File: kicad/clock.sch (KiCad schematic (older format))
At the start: 17 parts, among them P1 CONN_01X03, SW1 SWITCH_MIN, SW2 SWITCH_HR, U1 74LS90, U10 74LS247, U11 74LS73, U2 74LS90, U3 MAX6817, U4 74LS90, U5 74LS247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

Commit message: Add bypass caps and route VCC
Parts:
- added C1, C2: 22μF, Capacitors_SMD:C_0805_HandSoldering, symbol C
- renumbered C1 to C3, U8 to U7, U7 to U8
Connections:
- net GND: now also C1.2, C2.2
- net VCC: now also C1.1, C2.1
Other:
- note added: "C2012X6S0J226M085AC"
- moved on the sheet: C3, D1, P1, R1, SW1, SW2, U1, U2, U3

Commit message: Complete layout, pass DRC, create gerbers
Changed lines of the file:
@@
 Sheet 1 2
 Title "Clock"
-Date "2016-07-17"
-Rev "A"
+Date "2017-03-19"
+Rev "0.1"
 Comp "Scalez Inc."
 Comment1 ""
@@
 Connection ~ 16150 7500
 Wire Wire Line
-	16050 7500 16150 7500
-Wire Wire Line
-	16150 7500 16450 7500
+	16050 7500 16450 7500
 Wire Wire Line
 	16200 7300 17050 7300
@@
 	16100 8300 16100 6950
 Wire Wire Line
-	16050 7800 16200 7800
-Wire Wire Line
-	16200 7800 16450 7800
+	16050 7800 16450 7800
 Wire Wire Line
 	16450 7700 16050 7700
@@
 	16800 6850 16850 6850
 Wire Wire Line
-	16800 6600 16800 6650
-Wire Wire Line
-	16800 6650 16800 6850
+	16800 6600 16800 6850
 Wire Wire Line
 	16850 6650 16800 6650
@@
 	16850 6050 16650 6050
 Wire Wire Line
-	13450 7000 13450 7050
-Wire Wire Line
-	13450 7050 13450 7250
+	13450 7000 13450 7250
 Wire Wire Line
 	13500 7050 13450 7050
@@
 	11250 7700 11300 7700
 Wire Wire Line
-	11250 7450 11250 7500
-Wire Wire Line
-	11250 7500 11250 7700
+	11250 7450 11250 7700
 Wire Wire Line
 	11300 7500 11250 7500
 Wire Bus Line
-	11000 7000 11000 7100
-Wire Bus Line
-	11000 7100 11000 7200
-Wire Bus Line
-	11000 7200 11000 7300
-Wire Bus Line
-	11000 7300 11000 7600
-Wire Bus Line
-	11000 7600 11000 7700
-Wire Bus Line
-	11000 7700 11000 7800
-Wire Bus Line
-	11000 7800 11000 7900
+	11000 7000 11000 7900
 Wire Wire Line
 	11300 7000 11100 7000
@@
 	3150 7350 3100 7350
 Wire Wire Line
-	3100 7350 3100 7450
-Wire Wire Line
-	3100 7450 3100 7600
-Wire Wire Line
-	3100 7600 3100 7700
-Wire Wire Line
-	3100 7700 3100 7750
+	3100 7350 3100 7750
 Wire Wire Line
 	3100 7450 3150 7450
@@
 	11150 8350 11300 8350
 Wire Wire Line
-	9050 7950 9050 8050
-Wire Wire Line
-	9050 8050 9050 8200
-Wire Wire Line
-	9050 8200 9050 8300
-Wire Wire Line
-	9050 8300 9050 8350
+	9050 7950 9050 8350
 Connection ~ 9050 8050
 Connection ~ 9050 8200
@@
 	6400 7200 6400 7600
 Wire Wire Line
-	6250 7600 6400 7600
-Wire Wire Line
-	6400 7600 6700 7600
+	6250 7600 6700 7600
 Wire Wire Line
 	4750 7300 4750 7500
@@
 	4750 7500 4800 7500
 Wire Wire Line
-	4750 7900 4750 8000
-Wire Wire Line
-	4750 8000 4750 8050
+	4750 7900 4750 8050
 Wire Wire Line
 	3150 7200 3100 7200
@@
 	9050 7600 9050 7800
 Wire Wire Line
-	10550 7700 10600 7700
-Wire Wire Line
-	10600 7700 10900 7700
+	10550 7700 10900 7700
 Wire Wire Line
 	11300 8100 11250 8100
@@
 	11250 8100 11250 7900
 Wire Wire Line
-	12750 8000 12800 8000
-Wire Wire Line
-	12800 8000 13150 8000
-Wire Wire Line
-	10550 8000 10900 8000
-Wire Wire Line
-	10900 8000 11300 8000
+	12750 8000 13150 8000
+Wire Wire Line
+	10550 8000 11300 8000
 Connection ~ 6400 7600
 Wire Wire Line
 	4600 7400 4800 7400
 Wire Wire Line
-	2750 7100 3000 7100
-Wire Wire Line
-	3000 7100 3150 7100
+	2750 7100 3150 7100
 Wire Wire Line
 	10550 7900 10900 7900
@@
 	11200 7850 12850 7850
 Wire Wire Line
-	12750 8100 12850 8100
-Wire Wire Line
-	12850 8100 13150 8100
+	12750 8100 13150 8100
 Wire Wire Line
 	11150 8350 11150 7800
@@
 	12900 7800 12900 8200
 Wire Wire Line
-	11250 8500 11250 8600
-Wire Wire Line
-	11250 8600 11250 8650
+	11250 8500 11250 8650
 Connection ~ 12900 8200
 Wire Bus Line
-	13250 6550 13250 6650
-Wire Bus Line
-	13250 6650 13250 6750
-Wire Bus Line
-	13250 6750 13250 7900
-Wire Bus Line
-	13250 7900 13250 8000
-Wire Bus Line
-	13250 8000 13250 8100
-Wire Wire Line
-	14600 7500 14600 7600
-Wire Wire Line
-	14600 7600 14600 7700
-Wire Wire Line
-	14350 7500 14600 7500
-Wire Wire Line
-	14600 7500 14650 7500
+	13250 6550 13250 8100
+Wire Wire Line
+	14600 7500 14600 7700
+Wire Wire Line
+	14350 7500 14650 7500
 Wire Wire Line
 	14600 7600 14650 7600
@@
 	14500 8100 14650 8100
 Wire Wire Line
-	14500 7750 14500 7800
-Wire Wire Line
-	14500 7800 14500 8100
-Wire Wire Line
-	14500 8100 14500 8200
+	14500 7750 14500 8200
 Wire Wire Line
 	14500 7800 14650 7800
@@
 Connection ~ 14500 8100
 Wire Wire Line
-	16050 7600 16150 7600
-Wire Wire Line
-	16150 7600 16450 7600
+	16050 7600 16450 7600
 Wire Wire Line
 	14550 8000 14650 8000
@@
 Connection ~ 16150 7600
 Wire Bus Line
-	16550 6150 16550 6250
+	16550 6150 16550 6500
 Wire Bus Line
-	16550 6250 16550 6350
-Wire Bus Line
-	16550 6350 16550 6450
-Wire Bus Line
-	16550 6450 16550 6500
-Wire Bus Line
-	16550 6450 16550 7400
-Wire Bus Line
-	16550 7400 16550 7500
-Wire Bus Line
-	16550 7500 16550 7600
-Wire Bus Line
-	16550 7600 16550 7700
+	16550 6450 16550 7700
 Wire Wire Line
 	16150 7100 17050 7100
@@
 	19650 7100 19700 7100
 Wire Wire Line
-	19650 7100 19650 7500
-Wire Wire Line
-	19650 7500 19650 7900
-Wire Wire Line
-	19650 7900 19650 8000
-Wire Wire Line
-	19650 8000 19650 8400
-Wire Wire Line
-	19650 8400 19650 8800
+	19650 7100 19650 8800
 Wire Wire Line
 	19650 7500 19700 7500
@@
 	11300 6900 11100 6900
 Wire Wire Line
-	18250 7200 18300 7200
-Wire Wire Line
-	18300 7200 18400 7200
+	18250 7200 18400 7200
 Connection ~ 18300 7200
 Connection ~ 19650 7900
@@
 	18300 8600 18300 7200
 Wire Wire Line
-	18350 7400 18350 8200
-Wire Wire Line
-	18350 8200 18350 8650
-Wire Wire Line
-	18250 8200 18350 8200
-Wire Wire Line
-	18350 8200 19700 8200
+	18350 7400 18350 8650
+Wire Wire Line
+	18250 8200 19700 8200
 Connection ~ 18350 8200
 Wire Wire Line
@@
 	13300 8200 13250 8200
 Wire Wire Line
-	13250 8200 13250 8400
-Wire Wire Line
-	13250 8400 13250 8800
+	13250 8200 13250 8800
 Wire Wire Line
 	13250 8400 13300 8400
@@
 	7300 7950 7350 7950
 Wire Wire Line
-	6400 7800 6400 8200
-Wire Wire Line
-	6400 8200 6400 8300
+	6400 7800 6400 8300
 Wire Wire Line
 	8650 7700 9100 7700
@@
 	8850 8350 8850 8300
 Wire Wire Line
-	8850 7900 8850 7950
-Wire Wire Line
-	8850 7950 8850 8000
+	8850 7900 8850 8000
 Wire Wire Line
 	8650 7950 8850 7950
@@
 $EndComp
 Wire Wire Line
-	3000 7050 3000 7100
-Wire Wire Line
-	3000 7100 3000 8200
+	3000 7050 3000 8200
 Wire Wire Line
 	3000 6650 3000 6600
@@
 Connection ~ 6400 8200
 Wire Wire Line
-	12750 8200 12900 8200
-Wire Wire Line
-	12900 8200 13150 8200
+	12750 8200 13150 8200
 Text Label 6450 8100 0    60   ~ 0
 mto2
@@
 $EndComp
 Wire Wire Line
-	1900 6850 1900 6800
-Wire Wire Line
-	1900 6800 1800 6800
-Wire Wire Line
-	1800 6800 1700 6800
+	1900 6800 1900 6850
+Wire Wire Line
+	1700 6800 1900 6800
 Wire Wire Line
 	1700 6800 1700 6850
@@
 	1700 7150 1700 7200
 Wire Wire Line
-	1700 7200 1800 7200
-Wire Wire Line
-	1800 7200 1900 7200
+	1700 7200 1900 7200
 Wire Wire Line
 	1900 7200 1900 7150

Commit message: Add notes to schematic and update pcbnew view
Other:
- note added: "Seconds"
- moved on the sheet: C1, C2, C3, D1, P1, R1, SW1, SW2, U1, U10, U11A, U11B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

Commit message: Add BoM, update component info, use 150Ohm current limiting resistors, update layout respectively
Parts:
- C1, C2: Distrib Link (none) -> http://www.digikey.com/product-detail/en/tdk-corporation/C2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; Distrib PN (none) -> 445-14469-1-ND; MFG Name (none) -> TDK; MFG Part Num (none) -> C2012X6S0J226M085AC; Others (none) -> http://www.digikey.com/products/en/capacitors/ceramic-capac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; Tolerance (none) -> 20%
- C3: Distrib Link (none) -> http://www.digikey.com/product-detail/en/tdk-corporation/C2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; Distrib PN (none) -> 445-8883-1-ND; MFG Name (none) -> TDK; MFG Part Num (none) -> C2012X7T2E104K125AE; Others (none) -> http://www.digikey.com/products/en/capacitors/ceramic-capac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; Tolerance (none) -> 10%
- D1: Distrib Link (none) -> http://www.digikey.com/product-detail/en/lite-on-inc/LTST-C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; Distrib PN (none) -> 160-1427-1-ND; MFG Name (none) -> Lite-On; MFG Part Num (none) -> LTST-C171KRKT; Others (none) -> http://www.digikey.com/products/en/optoelectronics/led-indi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; Tolerance (none) -> -
- P1: Distrib Link (none) -> http://www.digikey.com/product-detail/en/molex-llc/07055300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; Distrib PN (none) -> WM4901-ND; MFG Name (none) -> Molex; MFG Part Num (none) -> 0705530002; Others (none) -> -; Tolerance (none) -> -
- R1: value 220Ω -> 150Ω; Distrib Link (none) -> http://www.digikey.com/product-detail/en/stackpole-electron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; Distrib PN (none) -> RMCF0805JT150RCT-ND; MFG Name (none) -> Stackpole Electronics; MFG Part Num (none) -> RMCF0805JT150R; Others (none) -> http://www.digikey.com/products/en/resistors/chip-resistor-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; Tolerance (none) -> 5%
- SW1, SW2: Distrib Link (none) -> http://www.digikey.com/product-detail/en/nkk-switches/AB15A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; Distrib PN (none) -> 360-2706-ND; MFG Name (none) -> NKK Switches; MFG Part Num (none) -> AB15AP-FA; Others (none) -> -; Tolerance (none) -> -
- U1, U2, U4, U6: Distrib Link (none) -> http://www.digikey.com/product-detail/en/texas-instruments/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; Distrib PN (none) -> 296-3746-5-ND; MFG Name (none) -> Texas Instruments; MFG Part Num (none) -> SN74LS90D; Others (none) -> http://www.digikey.com/products/en?keywords=74ls90&stock=1; Tolerance (none) -> -
- U10, U5, U8: Distrib Link (none) -> http://www.digikey.com/product-detail/en/texas-instruments/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; Distrib PN (none) -> 296-38241-1-ND; MFG Name (none) -> Texas Instruments; MFG Part Num (none) -> SN74LS247DR; Others (none) -> http://www.digikey.com/products/en?keywords=74ls247&stock=1; Tolerance (none) -> -
- U11: Distrib Link (none) -> http://www.digikey.com/product-detail/en/texas-instruments/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; Distrib PN (none) -> 296-3742-1-ND; MFG Name (none) -> Texas Instruments; MFG Part Num (none) -> SN74LS73ADR; Others (none) -> http://www.digikey.com/products/en?keywords=74LS73&stock=1; Tolerance (none) -> -
- U3: Distrib Link (none) -> http://www.digikey.com/product-detail/en/maxim-integrated/M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; Distrib PN (none) -> MAX6817EUT+TCT-ND; MFG Name (none) -> Maxim; MFG Part Num (none) -> MAX6817EUT+T; Others (none) -> http://www.digikey.com/products/en?keywords=MAX6817&stock=1; Tolerance (none) -> -
- U7: Distrib Link (none) -> http://www.digikey.com/product-detail/en/texas-instruments/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; Distrib PN (none) -> 296-14873-1-ND; MFG Name (none) -> Texas Instruments; MFG Part Num (none) -> SN74LS00DR; Others (none) -> http://www.digikey.com/products/en?keywords=74ls00&stock=1; Tolerance (none) -> -
- U9: Distrib Link (none) -> http://www.digikey.com/product-detail/en/texas-instruments/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; Distrib PN (none) -> 296-44704-1-ND; MFG Name (none) -> Texas Instruments; MFG Part Num (none) -> SN74LS163ADR; Others (none) -> http://www.digikey.com/products/en?keywords=74ls163&stock=1; Tolerance (none) -> -
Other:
- note removed: "C2012X6S0J226M085AC"

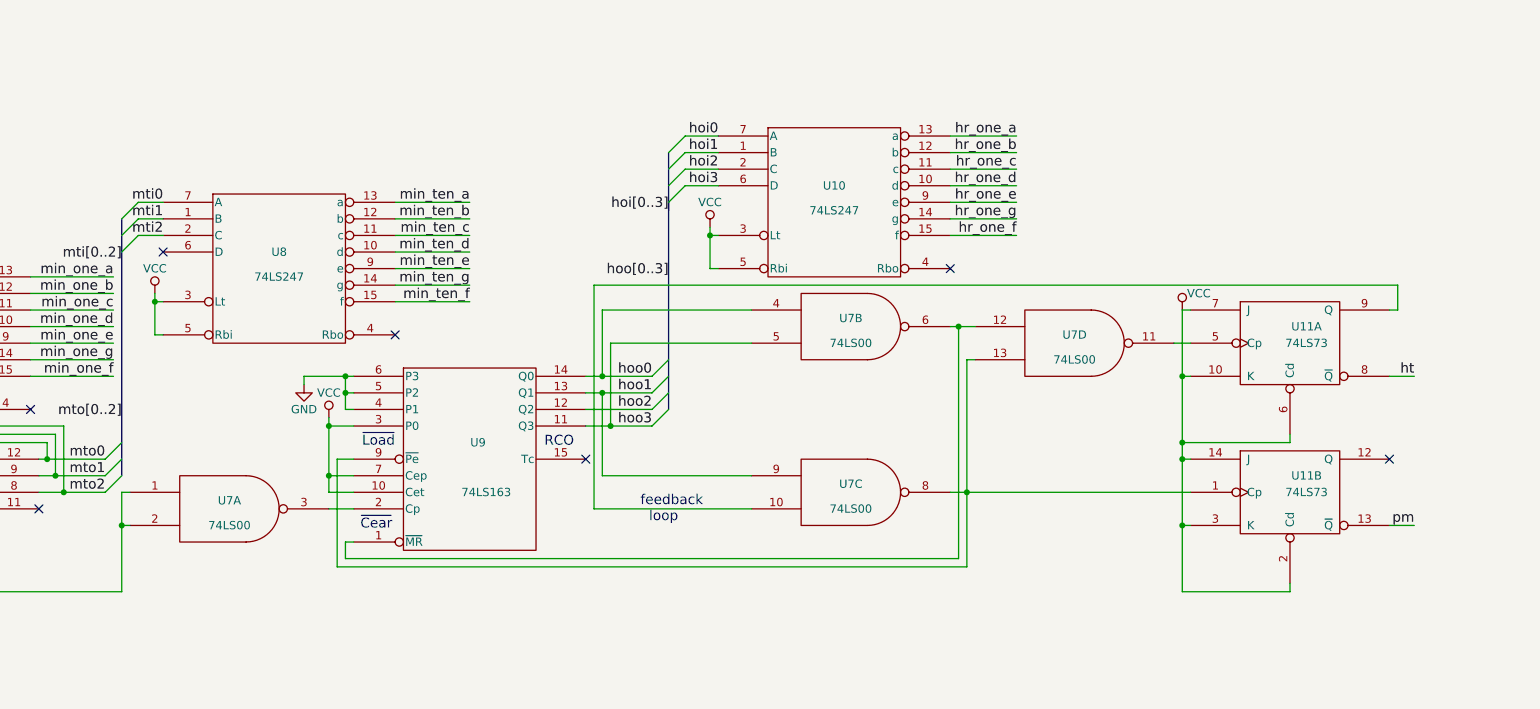
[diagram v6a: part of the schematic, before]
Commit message: Brint input D of U8 to GND
Was floating
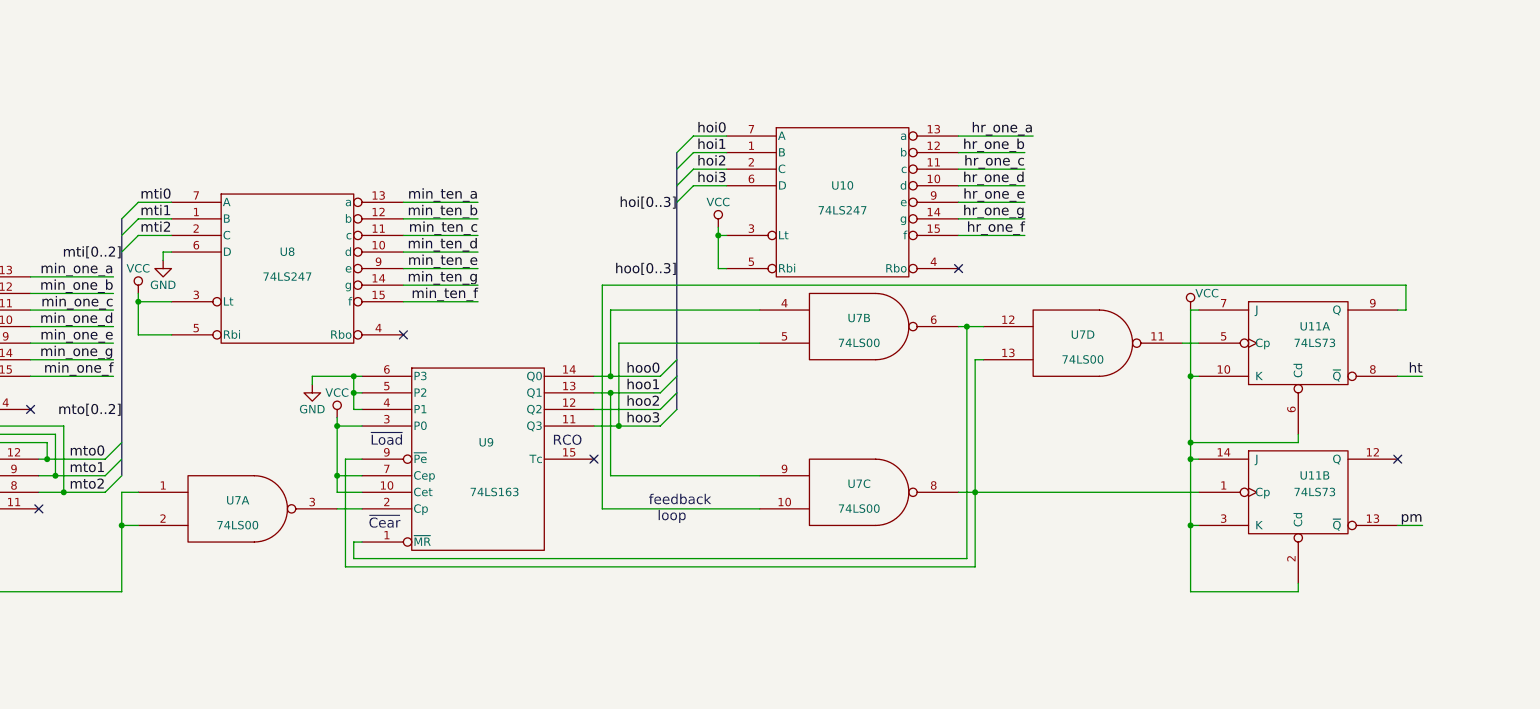
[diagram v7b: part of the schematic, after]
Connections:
- net GND: now also U8.6 (D)
- no-connect marks 10 -> 9
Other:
- moved on the sheet: U10, U11A, U11B, U7A, U7B, U7C, U7D, U8, U9

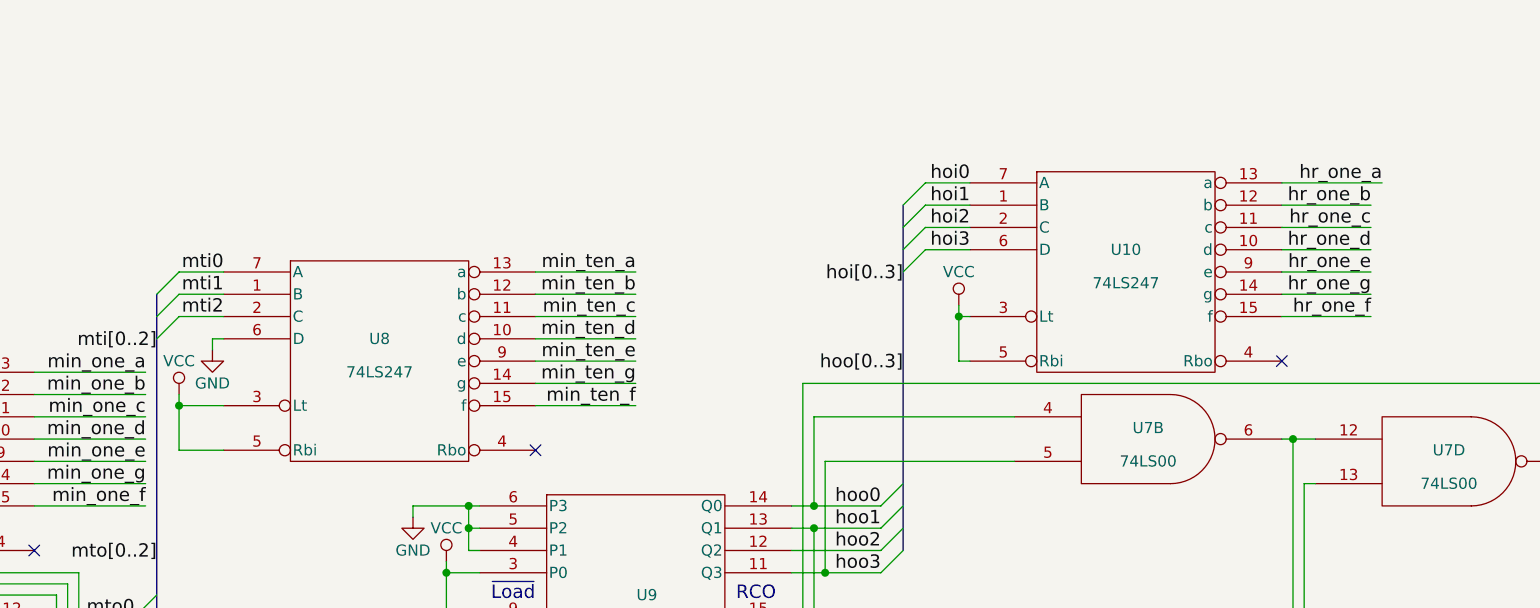
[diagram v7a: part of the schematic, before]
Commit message: Swap pin 1 and 3 of the SPDT push button footprint and update layout accordingly
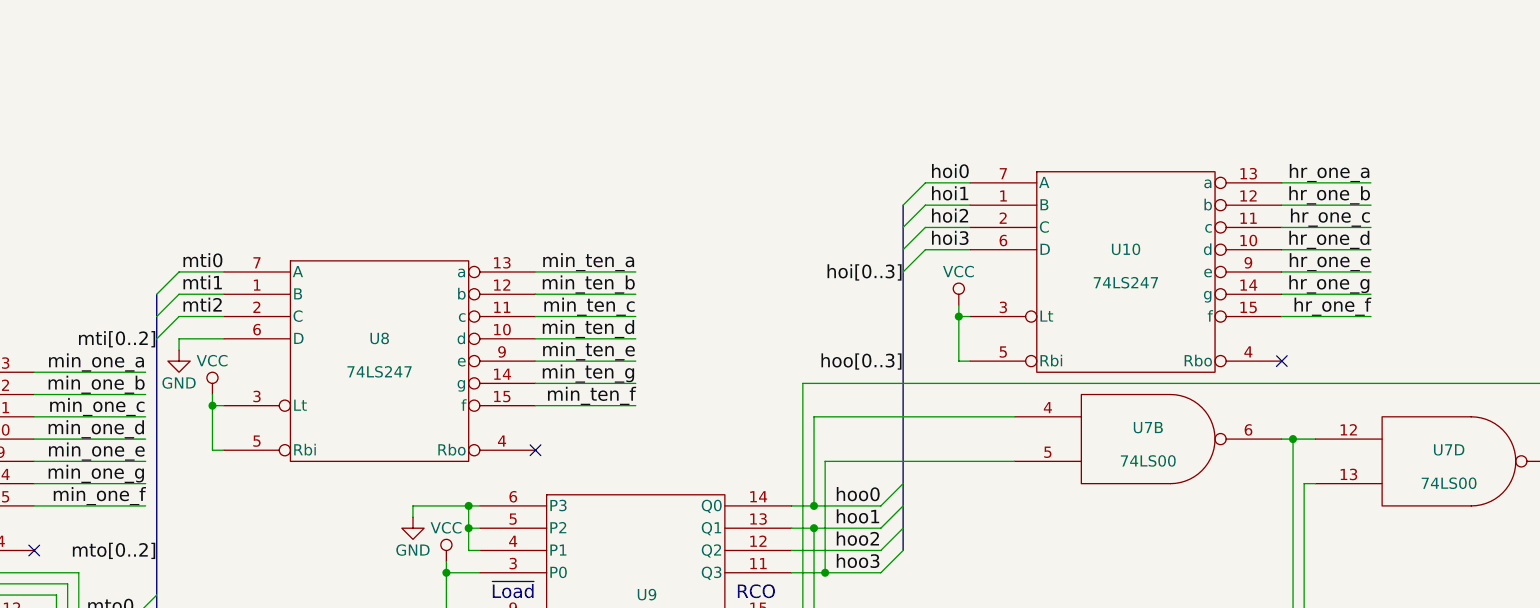
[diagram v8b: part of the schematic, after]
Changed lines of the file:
@@
 Text Label 15500 6950 2    60   ~ 0
 min_ten_g
-Text Label 18850 6050 2    60   ~ 0
+Text Label 18800 6050 2    60   ~ 0
 hr_one_a
 Text Label 18800 6150 2    60   ~ 0
@@
 L VCC #PWR011
 U 1 1 586B772B
-P 13450 7000
-F 0 "#PWR011" H 13450 6850 50  0001 C CNN
-F 1 "VCC" H 13450 7150 50  0000 C CNN
-F 2 "" H 13450 7000 50  0000 C CNN
-F 3 "" H 13450 7000 50  0000 C CNN
-	1    13450 7000
+P 13600 7000
+F 0 "#PWR011" H 13600 6850 50  0001 C CNN
+F 1 "VCC" H 13600 7150 50  0000 C CNN
+F 2 "" H 13600 7000 50  0000 C CNN
+F 3 "" H 13600 7000 50  0000 C CNN
+	1    13600 7000
 	1    0    0    -1
 $EndComp
@@
 L GND #PWR023
 U 1 1 58E55085
-P 13600 6800
-F 0 "#PWR023" H 13600 6550 50  0001 C CNN
-F 1 "GND" H 13600 6650 50  0000 C CNN
-F 2 "" H 13600 6800 50  0000 C CNN
-F 3 "" H 13600 6800 50  0000 C CNN
-	1    13600 6800
-	1    0    0    -1
-$EndComp
-Wire Wire Line
-	13600 6750 13600 6800
-Wire Wire Line
-	13650 6750 13600 6750
+P 13450 6800
+F 0 "#PWR023" H 13450 6550 50  0001 C CNN
+F 1 "GND" H 13450 6650 50  0000 C CNN
+F 2 "" H 13450 6800 50  0000 C CNN
+F 3 "" H 13450 6800 50  0000 C CNN
+	1    13450 6800
+	1    0    0    -1
+$EndComp
+Wire Wire Line
+	13450 6750 13450 6800
+Wire Wire Line
+	13650 6750 13450 6750
 Wire Wire Line
 	18400 6650 18800 6650
@@
 	18400 6150 18800 6150
 Wire Wire Line
-	18400 6050 18850 6050
+	18400 6050 18800 6050
 Wire Wire Line
 	12800 7500 13300 7500
@@
 	8950 8350 8950 8300
 Connection ~ 11350 7500
-Connection ~ 13450 7050
+Connection ~ 13600 7050
 Connection ~ 14650 7800
 Wire Wire Line
@@
 	21050 7100 21100 7100
 Wire Wire Line
-	13450 7250 13650 7250
+	13600 7250 13650 7250
 Wire Wire Line
 	13450 6650 13650 6650
@@
 	11350 7700 11400 7700
 Wire Wire Line
-	13650 7050 13450 7050
-Wire Wire Line
-	13450 7000 13450 7250
+	13650 7050 13600 7050
+Wire Wire Line
+	13600 7000 13600 7250
 Wire Wire Line
 	17000 6050 16800 6050
